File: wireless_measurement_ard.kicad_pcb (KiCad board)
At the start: 2 copper layers, 70 x 21.2 mm, 25 parts, among them J1 Conn_01x08, SW1 SW_SPDT, U1 EFM8LB1, U2 JDY-08, U3 MCP16415, U4 MAX9938, U5 MAX9938, U6 EFM8LB1x-QFP32

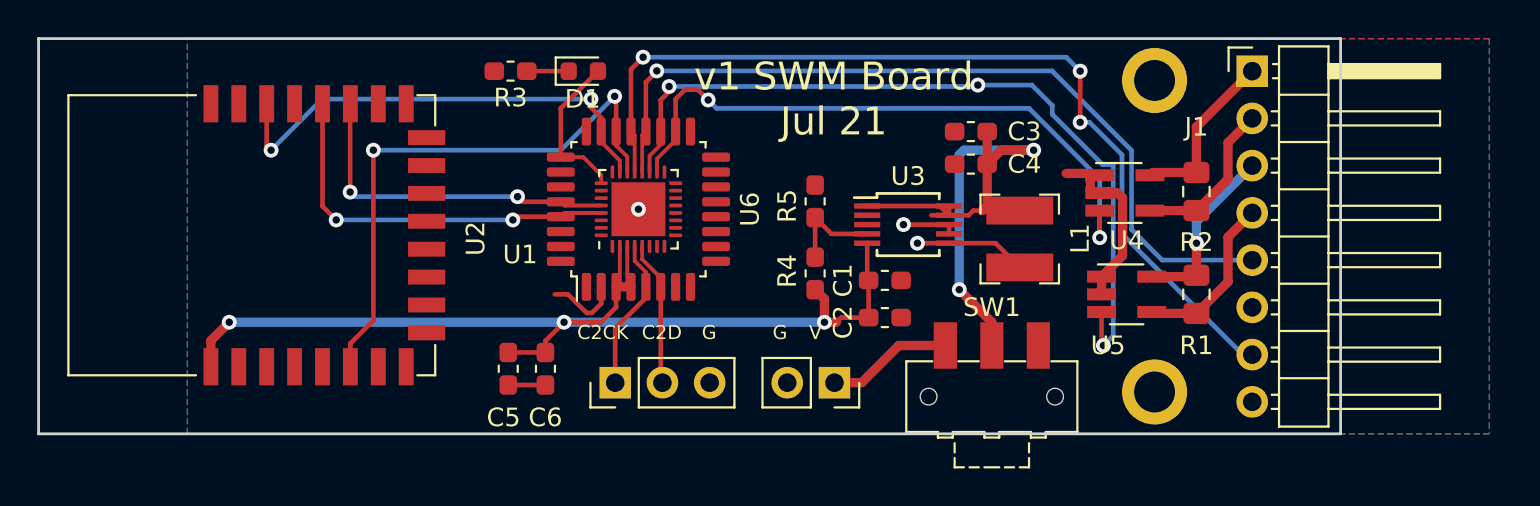
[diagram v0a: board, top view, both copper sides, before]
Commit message: updated footprint
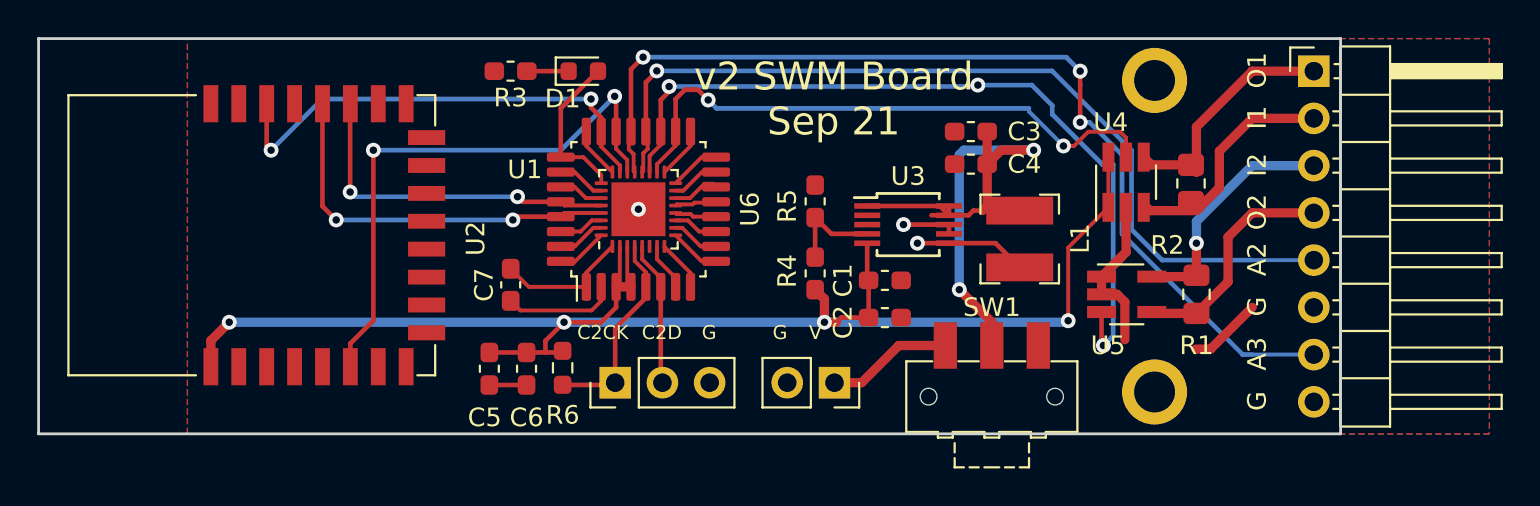
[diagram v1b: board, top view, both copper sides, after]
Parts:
- added C7: 4.7uF, Capacitor_SMD:C_0603_1608Metric_Pad1.08x0.95mm_HandSolder, F.Cu at (135.4, 88.2)
- added R6: 1k, Resistor_SMD:R_0603_1608Metric_Pad0.98x0.95mm_HandSolder, F.Cu at (138.2, 92.7)
- R2: value 5R3 -> 1R; footprint Resistor_SMD:R_0805_2012Metric_Pad1.15x1.40mm_HandSolder -> Resistor_SMD:R_0805_2012Metric_Pad1.20x1.40mm_HandSolder
- U4: value MAX9938 -> MAX44284; footprint Package_TO_SOT_SMD:SOT-23-5_HandSoldering -> Package_TO_SOT_SMD:SOT-23-6_Handsoldering
- moved J1 3.31 mm to (178.6, 76.8)
- moved C5 1.02 mm to (134.2, 92.8)
- moved C6 1.02 mm to (136.2, 92.8)
- moved U4 0.58 mm to (168.5, 82.7), turned to 90 degrees
- moved R2 0.53 mm to (172.0, 82.8)
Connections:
- J1 pad 1: C1_IN -> C1_OUT
- J1 pad 2: C1_OUT -> C1_IN
- R2 pad 1: C1_IN -> C1_OUT
- R2 pad 2: C1_OUT -> C1_IN
- U1 pad 1: Net-(U1-Pad1) -> P0.0
- U1 pad 10: Net-(U1-Pad10) -> P3.0
- U1 pad 11: Net-(U1-Pad11) -> P2.6
- U1 pad 12: Net-(U1-Pad12) -> P2.5
- U1 pad 13: Net-(U1-Pad13) -> P2.4
- U1 pad 14: Net-(U1-Pad14) -> P2.3
- U1 pad 15: Net-(U1-Pad15) -> P2.2
- U1 pad 16: Net-(U1-Pad16) -> P2.1
- U1 pad 17: Net-(U1-Pad17) -> P2.0
- U1 pad 24: Net-(U1-Pad24) -> P1.1
- U1 pad 26: Net-(U1-Pad26) -> P0.7
- U1 pad 27: Net-(U1-Pad27) -> P0.6
- U1 pad 30: Net-(U1-Pad30) -> P0.3
- U1 pad 31: Net-(U1-Pad31) -> P0.2
- U1 pad 32: Net-(U1-Pad32) -> P0.1
- U1 pad 7: Net-(U1-Pad7) -> P3.3
- U1 pad 8: Net-(U1-Pad8) -> P3.2
- U1 pad 9: Net-(U1-Pad9) -> P3.1
- U4 pad 1: GND -> +3V3
- U4 pad 3: A0 -> C1_IN
- U4 pad 5: C1_IN -> A0
- U6 pad 1: Net-(U6-Pad1) -> P0.0
- U6 pad 10: Net-(U6-Pad10) -> P3.0
- U6 pad 11: Net-(U6-Pad11) -> P2.6
- U6 pad 12: Net-(U6-Pad12) -> P2.5
- U6 pad 13: Net-(U6-Pad13) -> P2.4
- U6 pad 14: Net-(U6-Pad14) -> P2.3
- U6 pad 15: Net-(U6-Pad15) -> P2.2
- U6 pad 16: Net-(U6-Pad16) -> P2.1
- U6 pad 17: Net-(U6-Pad17) -> P2.0
- U6 pad 24: Net-(U6-Pad24) -> P1.1
- U6 pad 26: Net-(U6-Pad26) -> P0.7
- U6 pad 27: Net-(U6-Pad27) -> P0.6
- U6 pad 30: Net-(U6-Pad30) -> P0.3
- U6 pad 31: Net-(U6-Pad31) -> P0.2
- U6 pad 32: Net-(U6-Pad32) -> P0.1
- U6 pad 7: Net-(U6-Pad7) -> P3.3
- U6 pad 8: Net-(U6-Pad8) -> P3.2
- U6 pad 9: Net-(U6-Pad9) -> P3.1
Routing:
- net +3V3: track 56.9 -> 81.7 mm, vias 3 -> 4
- net P0.0: track 0.00 -> 7.23 mm
- net GND: track 18.2 -> 24.4 mm
- net C1_OUT: track 8.70 -> 12.7 mm
- net A3: track 50.0 -> 53.4 mm
- net A2: track 44.5 -> 47.9 mm
- net C2_OUT: track 9.08 -> 12.4 mm
- net C2_IN: track 9.57 -> 12.9 mm
- net C1_IN: track 9.25 -> 12.4 mm
- net C2CK: track 8.26 -> 11.1 mm
- net P2.1: track 0.00 -> 2.75 mm
- net P3.2: track 0.00 -> 2.75 mm
- net P3.1: track 0.00 -> 2.75 mm
- net P2.0: track 0.00 -> 2.75 mm
- net P1.1: track 0.00 -> 2.75 mm
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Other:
- board text added: "A2"
- board text added: "A3"
- board text added: "I1"
- board text added: "I2"
- board text added: "O1"
- board text added: "O2"
- board text added: "v2 SWM Board Sep 21"
- board text removed: "v1 SWM Board Jul 21"
